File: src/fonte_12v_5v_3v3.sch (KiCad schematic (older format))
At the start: 8 parts

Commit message: Verificação ERC -- checagem de erros elétricos no esquema -- concluída com sucesso. Há apenas dois warnings que não indicam problemas.
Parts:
- U2, U3: renamed from U?; footprint SOT-223 -> TO_SOT_Packages_SMD:SOT-223
- gave numbers to parts that had none: 6
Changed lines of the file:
@@
 $EndDescr
 $Comp
-L CONN_01X02 P?
+L CONN_01X02 P3
 U 1 1 57C9A160
 P 3500 3100
-F 0 "P?" H 3500 3250 50  0000 C CNN
+F 0 "P3" H 3500 3250 50  0000 C CNN
 F 1 "12V Connector" V 3600 3100 50  0000 C CNN
-F 2 "" H 3500 3100 50  0000 C CNN
+F 2 "" H 3500 3100 50  0001 C CNN
 F 3 "" H 3500 3100 50  0000 C CNN
 	1    3500 3100
@@
 $EndComp
 $Comp
-L GND #PWR?
+L GND #PWR06
 U 1 1 57C9A161
 P 7550 3900
-F 0 "#PWR?" H 7550 3650 50  0001 C CNN
+F 0 "#PWR06" H 7550 3650 50  0001 C CNN
 F 1 "GND" H 7550 3750 50  0000 C CNN
 F 2 "" H 7550 3900 50  0000 C CNN
@@
 $EndComp
 $Comp
-L GND #PWR?
+L GND #PWR07
 U 1 1 57C9A162
 P 4900 3900
-F 0 "#PWR?" H 4900 3650 50  0001 C CNN
+F 0 "#PWR07" H 4900 3650 50  0001 C CNN
 F 1 "GND" H 4900 3750 50  0000 C CNN
 F 2 "" H 4900 3900 50  0000 C CNN
@@
 $EndComp
 $Comp
-L GND #PWR?
+L GND #PWR08
 U 1 1 57C9A163
 P 3900 3400
-F 0 "#PWR?" H 3900 3150 50  0001 C CNN
+F 0 "#PWR08" H 3900 3150 50  0001 C CNN
 F 1 "GND" H 3900 3250 50  0000 C CNN
 F 2 "" H 3900 3400 50  0000 C CNN
@@
 $EndComp
 $Comp
-L D D?
+L D D2
 U 1 1 57C9A164
 P 4150 3050
-F 0 "D?" H 4150 3150 50  0000 C CNN
+F 0 "D2" H 4150 3150 50  0000 C CNN
 F 1 "1N4007" H 4150 2950 50  0000 C CNN
-F 2 "" H 4150 3050 50  0000 C CNN
+F 2 "" H 4150 3050 50  0001 C CNN
 F 3 "" H 4150 3050 50  0000 C CNN
 	1    4150 3050
@@
 $EndComp
 $Comp
-L +12V #PWR?
+L +12V #PWR09
 U 1 1 57C9A165
 P 4900 2800
-F 0 "#PWR?" H 4900 2650 50  0001 C CNN
+F 0 "#PWR09" H 4900 2650 50  0001 C CNN
 F 1 "+12V" H 4900 2940 50  0000 C CNN
 F 2 "" H 4900 2800 50  0000 C CNN
@@
 $EndComp
 $Comp
-L +5V #PWR?
+L +5V #PWR010
 U 1 1 57C9A166
 P 6800 2850
-F 0 "#PWR?" H 6800 2700 50  0001 C CNN
+F 0 "#PWR010" H 6800 2700 50  0001 C CNN
 F 1 "+5V" H 6800 2990 50  0000 C CNN
 F 2 "" H 6800 2850 50  0000 C CNN
@@
 $EndComp
 $Comp
-L LD1117S33CTR U?
+L LD1117S33CTR U3
 U 1 1 57C9A167
 P 7550 3100
-F 0 "U?" H 7550 3350 50  0000 C CNN
+F 0 "U3" H 7550 3350 50  0000 C CNN
 F 1 "LD1117S33CTR" H 7550 3300 50  0000 C CNN
-F 2 "SOT-223" H 7550 3200 50  0000 C CNN
+F 2 "TO_SOT_Packages_SMD:SOT-223" H 7550 3200 50  0000 C CNN
 F 3 "" H 7550 3100 50  0000 C CNN
 	1    7550 3100
@@
 $EndComp
 $Comp
-L LD1117S50CTR U?
+L LD1117S50CTR U2
 U 1 1 57C9A168
 P 6050 3100
-F 0 "U?" H 6050 3350 50  0000 C CNN
+F 0 "U2" H 6050 3350 50  0000 C CNN
 F 1 "LD1117S50CTR" H 6050 3300 50  0000 C CNN
-F 2 "SOT-223" H 6050 3200 50  0000 C CNN
+F 2 "TO_SOT_Packages_SMD:SOT-223" H 6050 3200 50  0000 C CNN
 F 3 "" H 6050 3100 50  0000 C CNN
 	1    6050 3100
@@
 $EndComp
 $Comp
-L CP C?
+L CP C1
 U 1 1 57C9A169
 P 4900 3550
-F 0 "C?" H 4925 3650 50  0000 L CNN
+F 0 "C1" H 4925 3650 50  0000 L CNN
 F 1 "220u16V" H 4925 3450 50  0000 L CNN
-F 2 "" H 4938 3400 50  0000 C CNN
+F 2 "" H 4938 3400 50  0001 C CNN
 F 3 "" H 4900 3550 50  0000 C CNN
 	1    4900 3550
@@
 $EndComp
 $Comp
-L CP C?
+L CP C2
 U 1 1 57C9A16A
 P 6800 3350
-F 0 "C?" H 6825 3450 50  0000 L CNN
+F 0 "C2" H 6825 3450 50  0000 L CNN
 F 1 "10u" H 6825 3250 50  0000 L CNN
-F 2 "" H 6838 3200 50  0000 C CNN
+F 2 "" H 6838 3200 50  0001 C CNN
 F 3 "" H 6800 3350 50  0000 C CNN
 	1    6800 3350
@@
 $EndComp
 $Comp
-L CP C?
+L CP C3
 U 1 1 57C9A16B
 P 8300 3300
-F 0 "C?" H 8325 3400 50  0000 L CNN
+F 0 "C3" H 8325 3400 50  0000 L CNN
 F 1 "10u" H 8325 3200 50  0000 L CNN
-F 2 "" H 8338 3150 50  0000 C CNN
+F 2 "" H 8338 3150 50  0001 C CNN
 F 3 "" H 8300 3300 50  0000 C CNN
 	1    8300 3300
@@
 $EndComp
 $Comp
-L GND #PWR?
+L GND #PWR011
 U 1 1 57C9A16C
 P 6800 3600
-F 0 "#PWR?" H 6800 3350 50  0001 C CNN
+F 0 "#PWR011" H 6800 3350 50  0001 C CNN
 F 1 "GND" H 6800 3450 50  0000 C CNN
 F 2 "" H 6800 3600 50  0000 C CNN
@@
 $EndComp
 $Comp
-L GND #PWR?
+L GND #PWR012
 U 1 1 57C9A16D
 P 6050 3450
-F 0 "#PWR?" H 6050 3200 50  0001 C CNN
+F 0 "#PWR012" H 6050 3200 50  0001 C CNN
 F 1 "GND" H 6050 3300 50  0000 C CNN
 F 2 "" H 6050 3450 50  0000 C CNN
@@
 $EndComp
 $Comp
-L +3.3V #PWR?
+L +3.3V #PWR013
 U 1 1 57C9A16E
 P 8300 2900
-F 0 "#PWR?" H 8300 2750 50  0001 C CNN
+F 0 "#PWR013" H 8300 2750 50  0001 C CNN
 F 1 "+3.3V" H 8300 3040 50  0000 C CNN
 F 2 "" H 8300 2900 50  0000 C CNN
@@
 $EndComp
 $Comp
-L D D?
+L D D1
 U 1 1 57CA12AC
 P 4150 2750
-F 0 "D?" H 4150 2850 50  0000 C CNN
+F 0 "D1" H 4150 2850 50  0000 C CNN
 F 1 "1N4007" H 4150 2650 50  0000 C CNN
-F 2 "" H 4150 2750 50  0000 C CNN
+F 2 "" H 4150 2750 50  0001 C CNN
 F 3 "" H 4150 2750 50  0000 C CNN
 	1    4150 2750

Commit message: Footprint atualizado
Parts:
- C1: footprint (none) -> Capacitores:Cap_Eletrolitico_8x5
- C2, C3: footprint (none) -> Capacitores:Cap_Eletrolitico_8x3.5
- D1, D2: footprint (none) -> Diodes_ThroughHole:Diode_DO-41_SOD81_Horizontal_RM10
- P3: footprint (none) -> Connect:BARREL_JACK
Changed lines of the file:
@@
 F 0 "P3" H 3500 3250 50  0000 C CNN
 F 1 "12V Connector" V 3600 3100 50  0000 C CNN
-F 2 "" H 3500 3100 50  0001 C CNN
+F 2 "Connect:BARREL_JACK" H 3500 3100 50  0001 C CNN
 F 3 "" H 3500 3100 50  0000 C CNN
 	1    3500 3100
@@
 F 0 "D2" H 4150 3150 50  0000 C CNN
 F 1 "1N4007" H 4150 2950 50  0000 C CNN
-F 2 "" H 4150 3050 50  0001 C CNN
+F 2 "Diodes_ThroughHole:Diode_DO-41_SOD81_Horizontal_RM10" H 4150 3050 50  0001 C CNN
 F 3 "" H 4150 3050 50  0000 C CNN
 	1    4150 3050
@@
 F 0 "C1" H 4925 3650 50  0000 L CNN
 F 1 "220u16V" H 4925 3450 50  0000 L CNN
-F 2 "" H 4938 3400 50  0001 C CNN
+F 2 "Capacitores:Cap_Eletrolitico_8x5" H 4938 3400 50  0001 C CNN
 F 3 "" H 4900 3550 50  0000 C CNN
 	1    4900 3550
@@
 F 0 "C2" H 6825 3450 50  0000 L CNN
 F 1 "10u" H 6825 3250 50  0000 L CNN
-F 2 "" H 6838 3200 50  0001 C CNN
+F 2 "Capacitores:Cap_Eletrolitico_8x3.5" H 6838 3200 50  0001 C CNN
 F 3 "" H 6800 3350 50  0000 C CNN
 	1    6800 3350
@@
 F 0 "C3" H 8325 3400 50  0000 L CNN
 F 1 "10u" H 8325 3200 50  0000 L CNN
-F 2 "" H 8338 3150 50  0001 C CNN
+F 2 "Capacitores:Cap_Eletrolitico_8x3.5" H 8338 3150 50  0001 C CNN
 F 3 "" H 8300 3300 50  0000 C CNN
 	1    8300 3300
@@
 F 0 "D1" H 4150 2850 50  0000 C CNN
 F 1 "1N4007" H 4150 2650 50  0000 C CNN
-F 2 "" H 4150 2750 50  0001 C CNN
+F 2 "Diodes_ThroughHole:Diode_DO-41_SOD81_Horizontal_RM10" H 4150 2750 50  0001 C CNN
 F 3 "" H 4150 2750 50  0000 C CNN
 	1    4150 2750

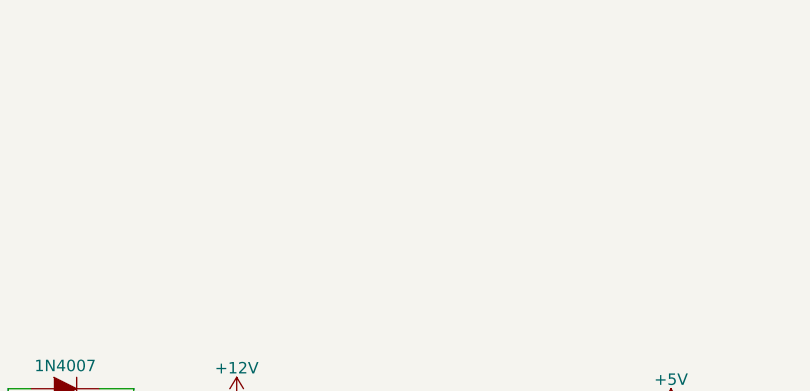
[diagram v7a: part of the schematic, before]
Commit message: PCB completa, feita a primeira revisão.
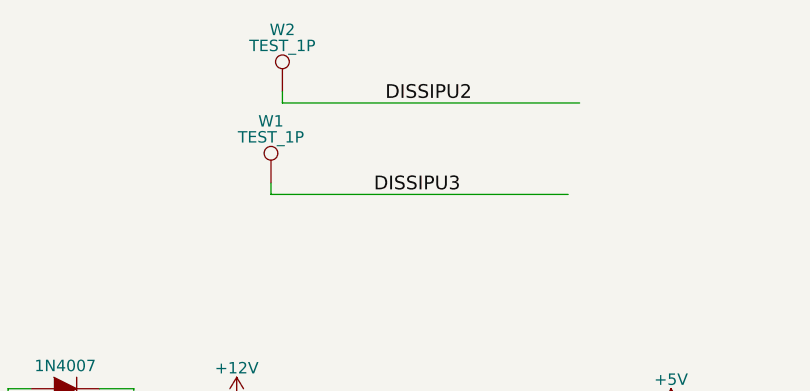
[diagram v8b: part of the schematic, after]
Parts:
- added W1, W2: TEST_1P, SMD_Packages:1Pin, symbol TEST_1P
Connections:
- net labels added: DISSIPU2, DISSIPU3
- wire segments 19 -> 23
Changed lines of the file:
@@
 $EndComp
 $Comp
-L GND #PWR06
+L GND #PWR08
 U 1 1 57C9A161
 P 7550 3900
-F 0 "#PWR06" H 7550 3650 50  0001 C CNN
+F 0 "#PWR08" H 7550 3650 50  0001 C CNN
 F 1 "GND" H 7550 3750 50  0000 C CNN
 F 2 "" H 7550 3900 50  0000 C CNN
@@
 $EndComp
 $Comp
-L GND #PWR07
+L GND #PWR09
 U 1 1 57C9A162
 P 4900 3900
-F 0 "#PWR07" H 4900 3650 50  0001 C CNN
+F 0 "#PWR09" H 4900 3650 50  0001 C CNN
 F 1 "GND" H 4900 3750 50  0000 C CNN
 F 2 "" H 4900 3900 50  0000 C CNN
@@
 $EndComp
 $Comp
-L GND #PWR08
+L GND #PWR010
 U 1 1 57C9A163
 P 3900 3400
-F 0 "#PWR08" H 3900 3150 50  0001 C CNN
+F 0 "#PWR010" H 3900 3150 50  0001 C CNN
 F 1 "GND" H 3900 3250 50  0000 C CNN
 F 2 "" H 3900 3400 50  0000 C CNN
@@
 $EndComp
 $Comp
-L +12V #PWR09
+L +12V #PWR011
 U 1 1 57C9A165
 P 4900 2800
-F 0 "#PWR09" H 4900 2650 50  0001 C CNN
+F 0 "#PWR011" H 4900 2650 50  0001 C CNN
 F 1 "+12V" H 4900 2940 50  0000 C CNN
 F 2 "" H 4900 2800 50  0000 C CNN
@@
 $EndComp
 $Comp
-L +5V #PWR010
+L +5V #PWR012
 U 1 1 57C9A166
 P 6800 2850
-F 0 "#PWR010" H 6800 2700 50  0001 C CNN
+F 0 "#PWR012" H 6800 2700 50  0001 C CNN
 F 1 "+5V" H 6800 2990 50  0000 C CNN
 F 2 "" H 6800 2850 50  0000 C CNN
@@
 $EndComp
 $Comp
-L GND #PWR011
+L GND #PWR013
 U 1 1 57C9A16C
 P 6800 3600
-F 0 "#PWR011" H 6800 3350 50  0001 C CNN
+F 0 "#PWR013" H 6800 3350 50  0001 C CNN
 F 1 "GND" H 6800 3450 50  0000 C CNN
 F 2 "" H 6800 3600 50  0000 C CNN
@@
 $EndComp
 $Comp
-L GND #PWR012
+L GND #PWR014
 U 1 1 57C9A16D
 P 6050 3450
-F 0 "#PWR012" H 6050 3200 50  0001 C CNN
+F 0 "#PWR014" H 6050 3200 50  0001 C CNN
 F 1 "GND" H 6050 3300 50  0000 C CNN
 F 2 "" H 6050 3450 50  0000 C CNN
@@
 $EndComp
 $Comp
-L +3.3V #PWR013
+L +3.3V #PWR015
 U 1 1 57C9A16E
 P 8300 2900
-F 0 "#PWR013" H 8300 2750 50  0001 C CNN
+F 0 "#PWR015" H 8300 2750 50  0001 C CNN
 F 1 "+3.3V" H 8300 3040 50  0000 C CNN
 F 2 "" H 8300 2900 50  0000 C CNN
@@
 	3900 2750 3900 3050
 Connection ~ 3900 3050
+$Comp
+L TEST_1P W2
+U 1 1 57E48B67
+P 5100 1450
+F 0 "W2" H 5100 1720 50  0000 C CNN
+F 1 "TEST_1P" H 5100 1650 50  0000 C CNN
+F 2 "SMD_Packages:1Pin" H 5300 1450 50  0001 C CNN
+F 3 "" H 5300 1450 50  0000 C CNN
+	1    5100 1450
+	1    0    0    -1
+$EndComp
+Text Label 5550 1500 0    60   ~ 0
+DISSIPU2
+Wire Wire Line
+	5100 1450 5100 1500
+Wire Wire Line
+	5100 1500 6400 1500
+$Comp
+L TEST_1P W1
+U 1 1 57E48EB9
+P 5050 1850
+F 0 "W1" H 5050 2120 50  0000 C CNN
+F 1 "TEST_1P" H 5050 2050 50  0000 C CNN
+F 2 "SMD_Packages:1Pin" H 5250 1850 50  0001 C CNN
+F 3 "" H 5250 1850 50  0000 C CNN
+	1    5050 1850
+	1    0    0    -1
+$EndComp
+Text Label 5500 1900 0    60   ~ 0
+DISSIPU3
+Wire Wire Line
+	5050 1850 5050 1900
+Wire Wire Line
+	5050 1900 6350 1900
 $EndSCHEMATC
